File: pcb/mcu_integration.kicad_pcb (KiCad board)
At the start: 4 copper layers, 90.2 x 95.9 mm, 104 parts, among them IC1 TL7660IDGKR, IC10 AD844_OPAMP_MEL, IC2 TL081IDT, IC3 FOD814_OPTO_NOSHD, IC5 FOD814_OPTO_MEL, IC6 AD844_OPAMP_AL, IC7 FOD814_OPTO_AL, IC8 AD844_OPAMP_NOSHD, IC9 TL081IDT, J4 Conn_01x02, J5 DM3BT-DSF-PEJS, M1 MountingHole_Pad, M2 MountingHole_Pad, M3 MountingHole_Pad, M4 MountingHole_Pad, U1 STM32F103RBTx, U2 REF192_NOSHD, U3 REF192_AL, U4 REF192_MEL, U5 TPS2069CDBVR_MOSFET, U6 LM35DM

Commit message: Fixed PCB silkscreen
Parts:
- moved C45 0.19 mm to (156.0, 69.6)
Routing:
- net GND: track 183.5 -> 182.1 mm

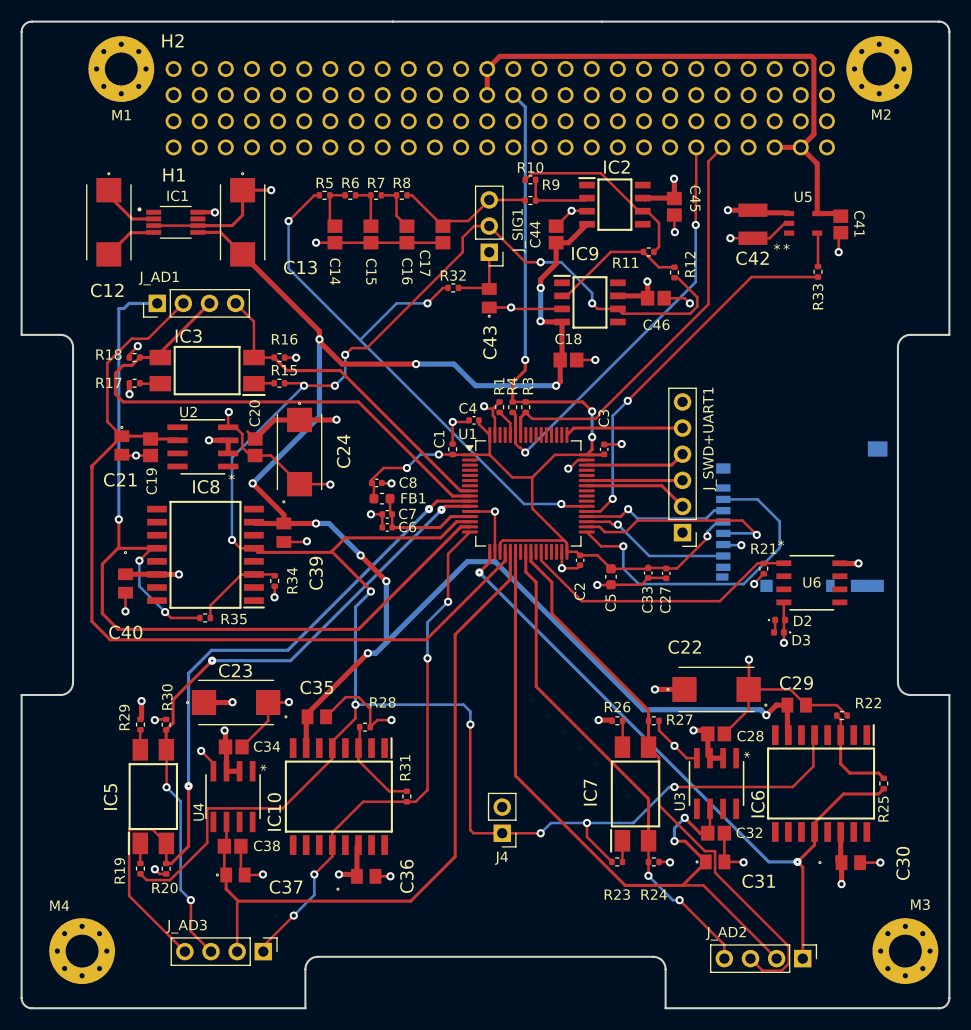
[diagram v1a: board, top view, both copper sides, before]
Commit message: Added silkscreen and changed diode footprints
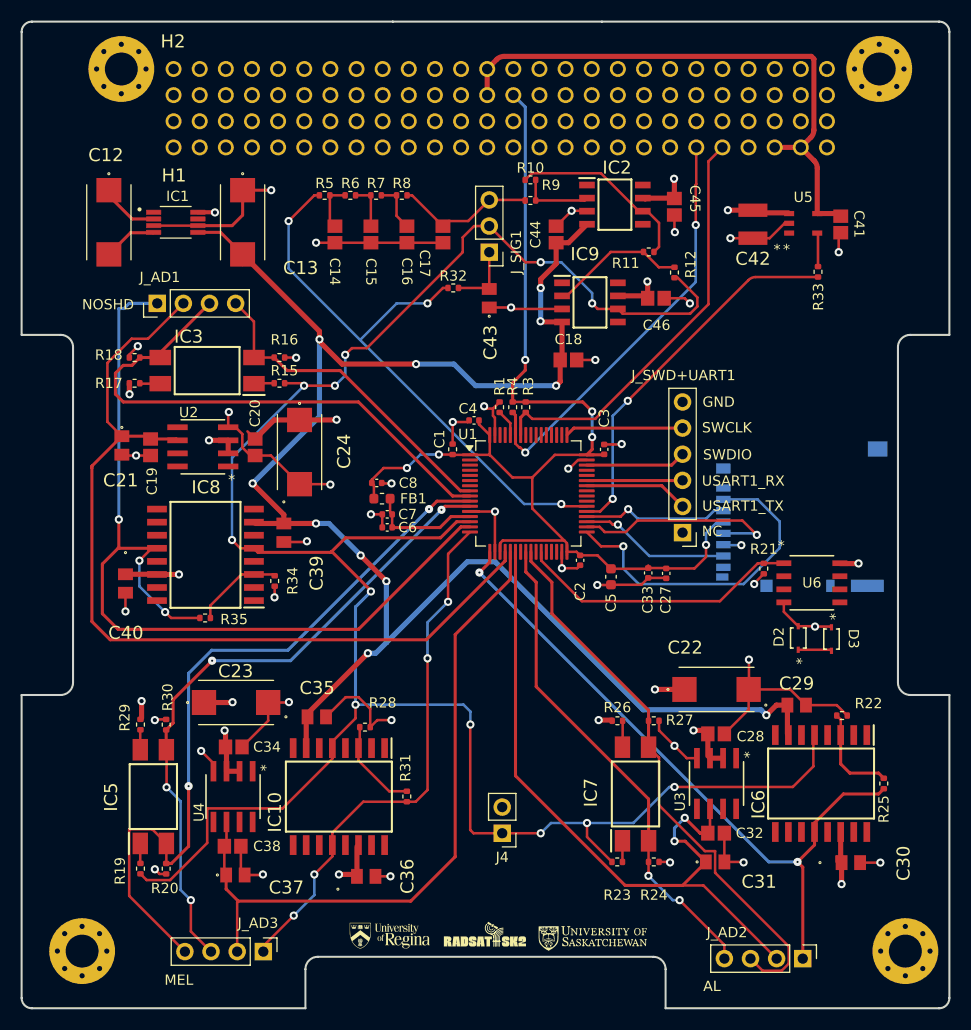
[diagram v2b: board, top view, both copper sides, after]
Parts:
- D2, D3: footprint Diode_SMD:D_0402_1005Metric -> capstone:SOD-323_1P7X1P25_ONS
- moved D3 5.15 mm to (171.3, 111.6), turned to -90 degrees
- moved D2 2.48 mm to (168.0, 111.5), turned to 90 degrees
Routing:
- net GND: track 182.1 -> 184.3 mm
- net DIODE_NET: track 1.41 -> 3.27 mm
- net 3.3V Output: track 109.1 -> 110.1 mm
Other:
- board text added: "AL"
- board text added: "CUBICS Analog IC Shielding Payload REV C Hunter Gerbrandt, Owen Markewich"
- board text added: "GND"
- board text added: "MEL"
- board text added: "NC"
- board text added: "NOSHD"
- board text added: "SWCLK"
- board text added: "SWDIO"
- board text added: "USART1_RX"
- board text added: "USART1_TX"

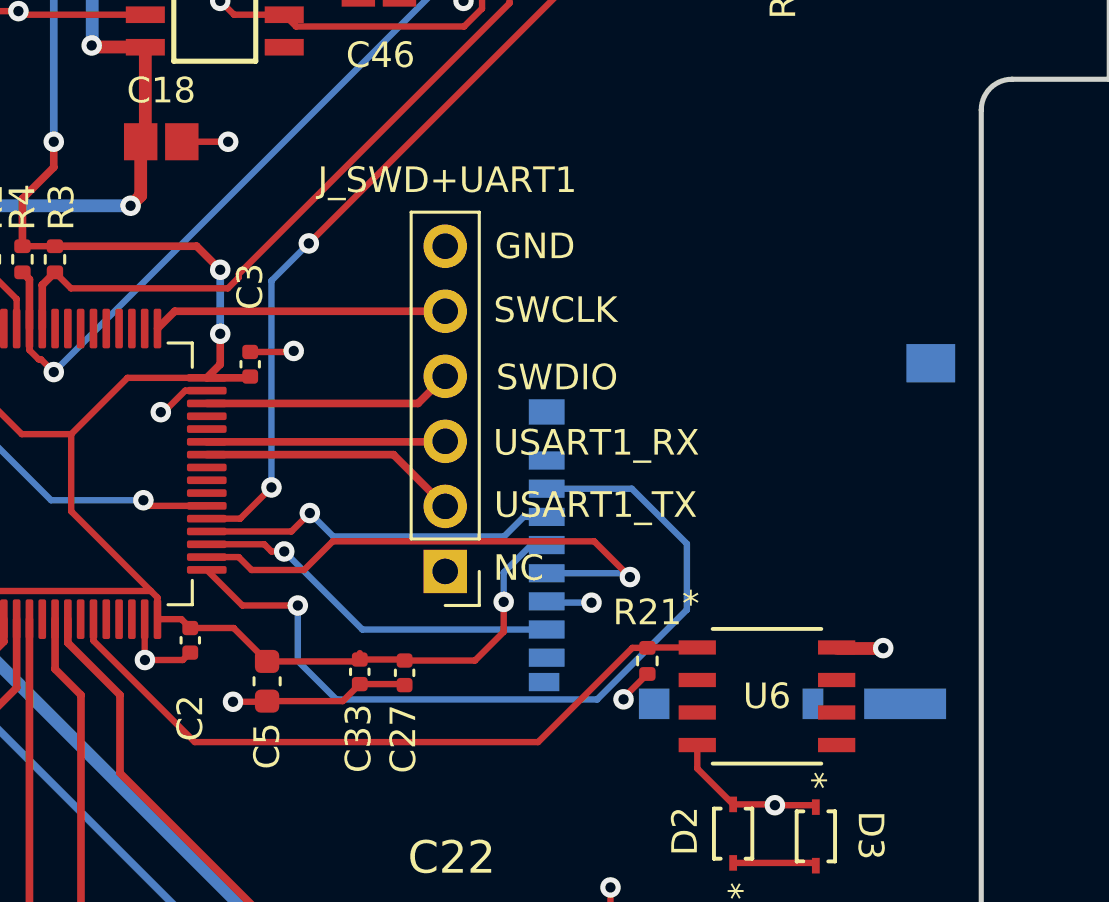
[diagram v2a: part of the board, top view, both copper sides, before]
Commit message: Added reset button & LED, fixed SD card overhang
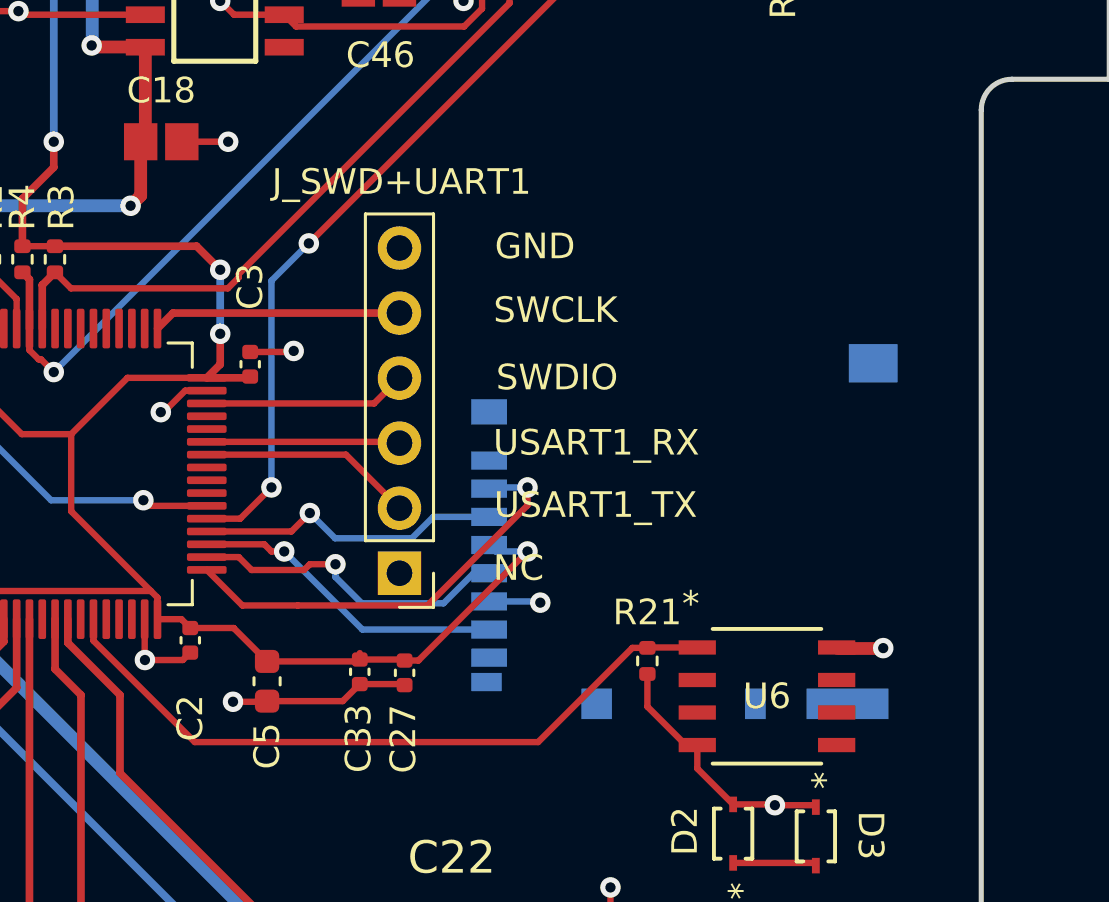
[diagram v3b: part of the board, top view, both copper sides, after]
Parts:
- C14, C15, C16, C17: value 0.1u -> 0.01u
- moved J5 2.25 mm to (166.3, 99.7)
- moved J_SWD+UART1 1.79 mm to (155.0, 101.3)
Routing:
- net /SPI2_CS_NSS: track 32.5 -> 16.9 mm
- net /SPI2_SCK: track 21.1 -> 12.7 mm
- net GND: track 184.3 -> 186.8 mm, vias 41 -> 40
- net /SPI2_MISO: track 14.7 -> 12.4 mm
- net /SPI2_MOSI: track 14.3 -> 12.1 mm
- net /SWDIO: track 9.75 -> 7.94 mm
- net /SWCLK: track 11.5 -> 9.70 mm
- net /USART1_RX: track 9.32 -> 7.55 mm
- net /USART1_TX: track 10.1 -> 8.39 mm
- net 3.3V Output: track 110.1 -> 109.5 mm

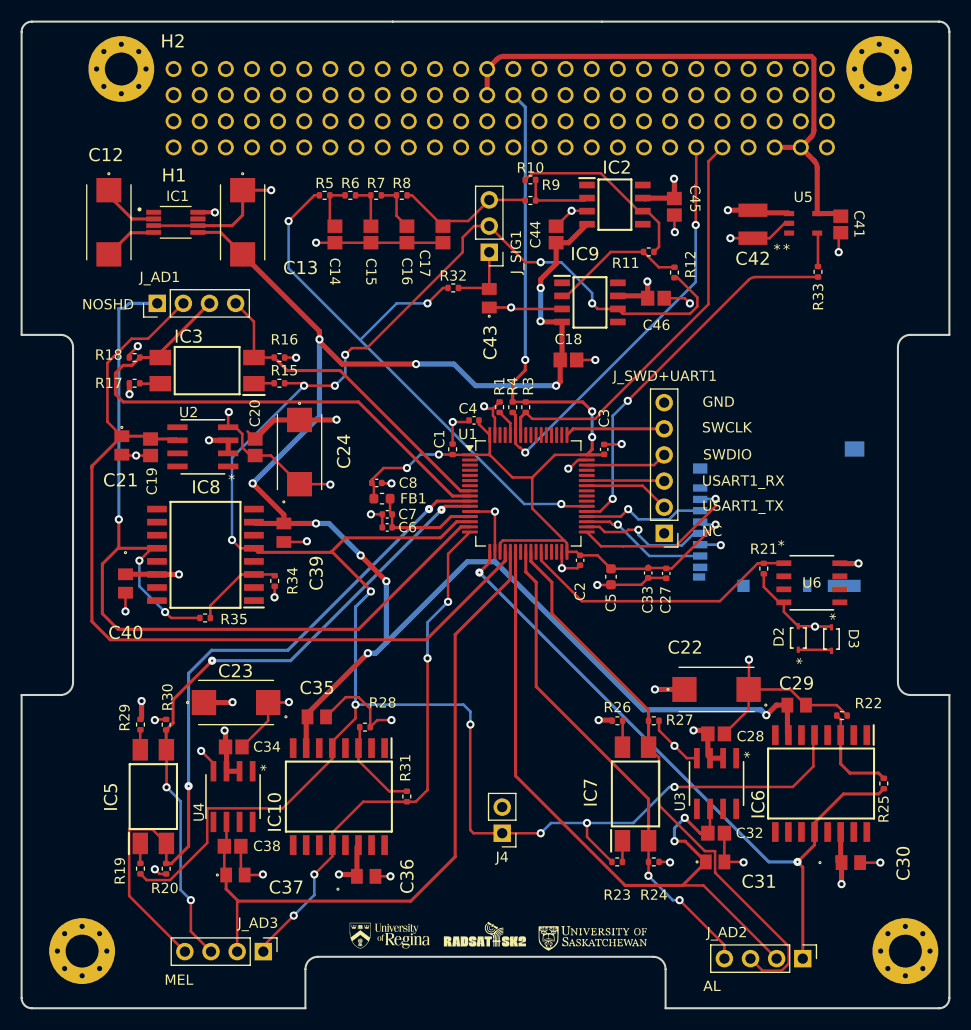
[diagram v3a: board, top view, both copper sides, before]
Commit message: Added reset button & LED, fixed SD card overhang
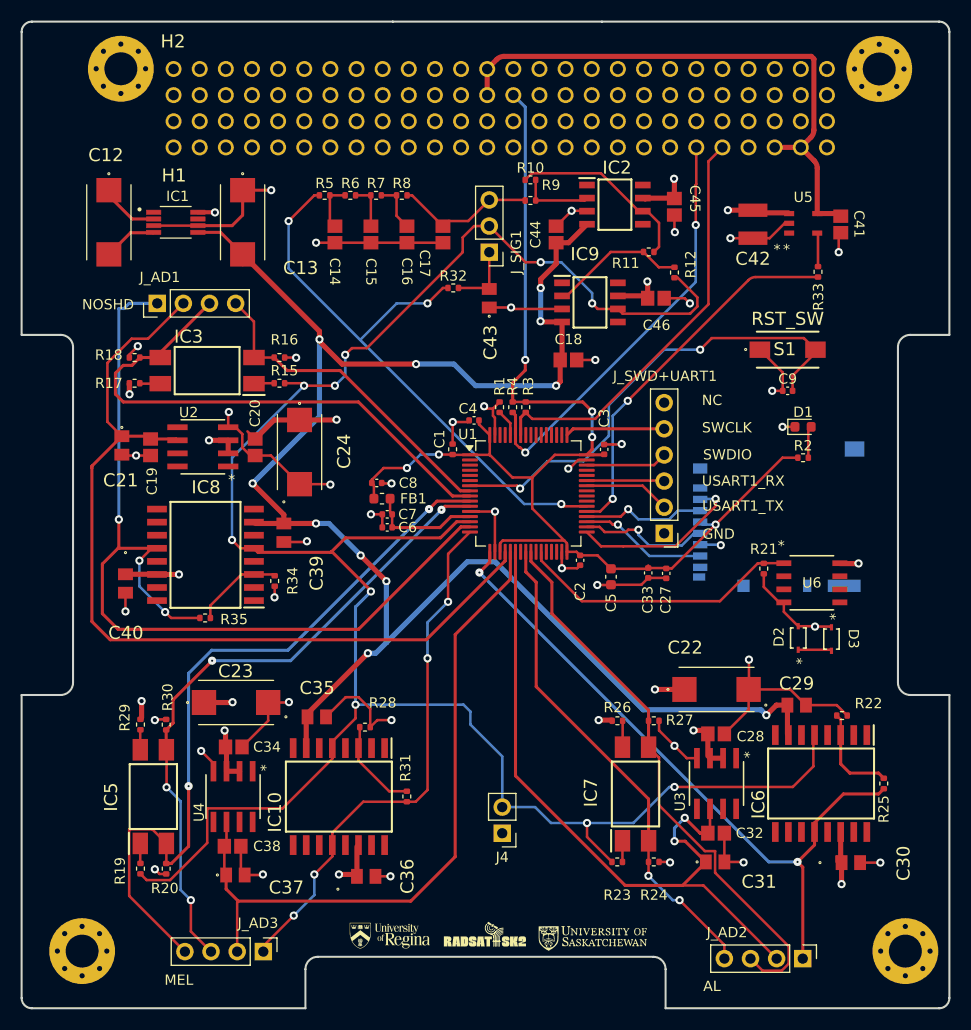
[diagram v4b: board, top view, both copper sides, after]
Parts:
- added C9: 100n, Capacitor_SMD:C_0402_1005Metric, F.Cu at (167.0, 87.5)
- added D1: RED, LED_SMD:LED_0603_1608Metric, F.Cu at (168.5, 91.0)
- added R2: 2.2k, Resistor_SMD:R_0402_1005Metric, F.Cu at (168.5, 94.0)
- added S1: RST_SW, capstone:95C04A3GWRT, F.Cu at (167.0, 83.5)
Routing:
- net /NRST: track 0.00 -> 46.9 mm, vias 0 -> 2
- net 3.3V Output: track 109.5 -> 120.2 mm
- net GND: track 186.8 -> 193.9 mm, vias 40 -> 42
- net ADC1_IN0_SINE: track 215.7 -> 211.8 mm, vias 12 -> 10
- net Net-(D1-A): track 0.00 -> 3.11 mm

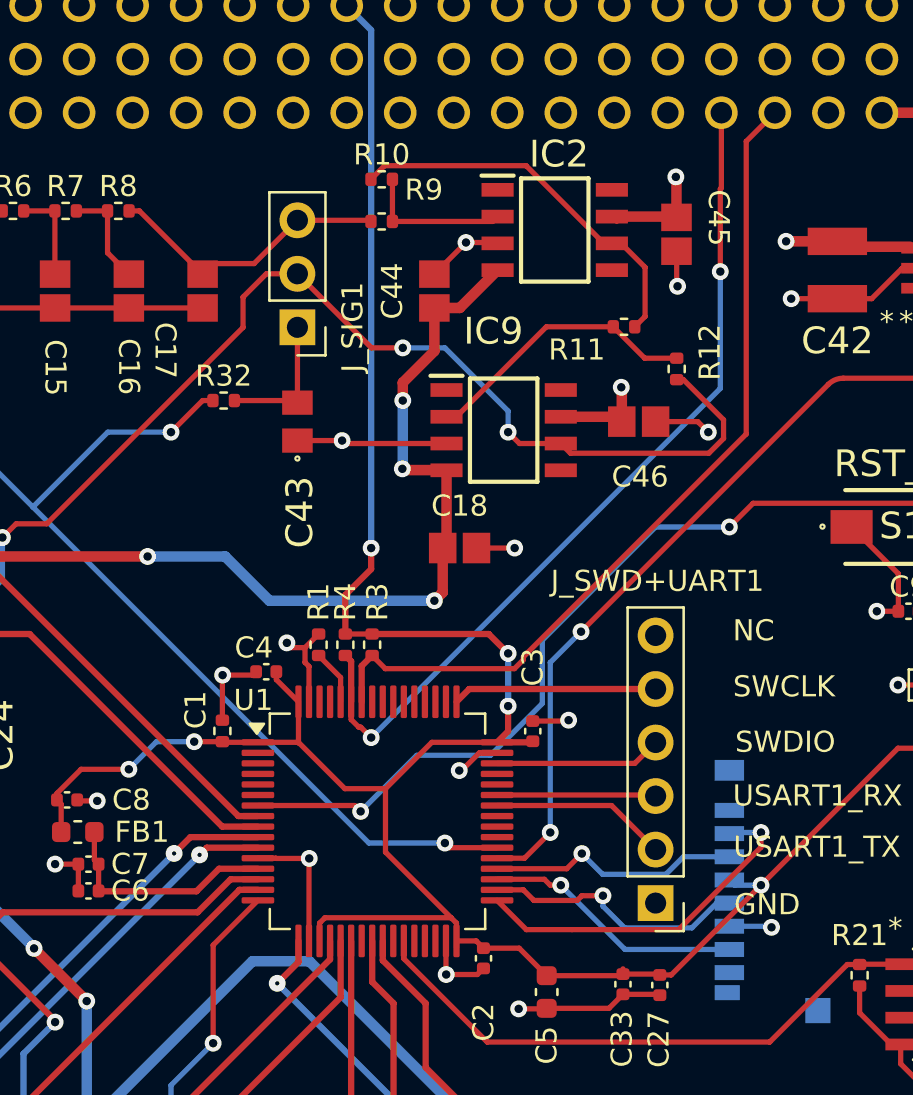
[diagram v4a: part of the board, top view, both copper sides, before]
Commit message: Added non-inverting amplifier to RC Ladder and Changed header pin
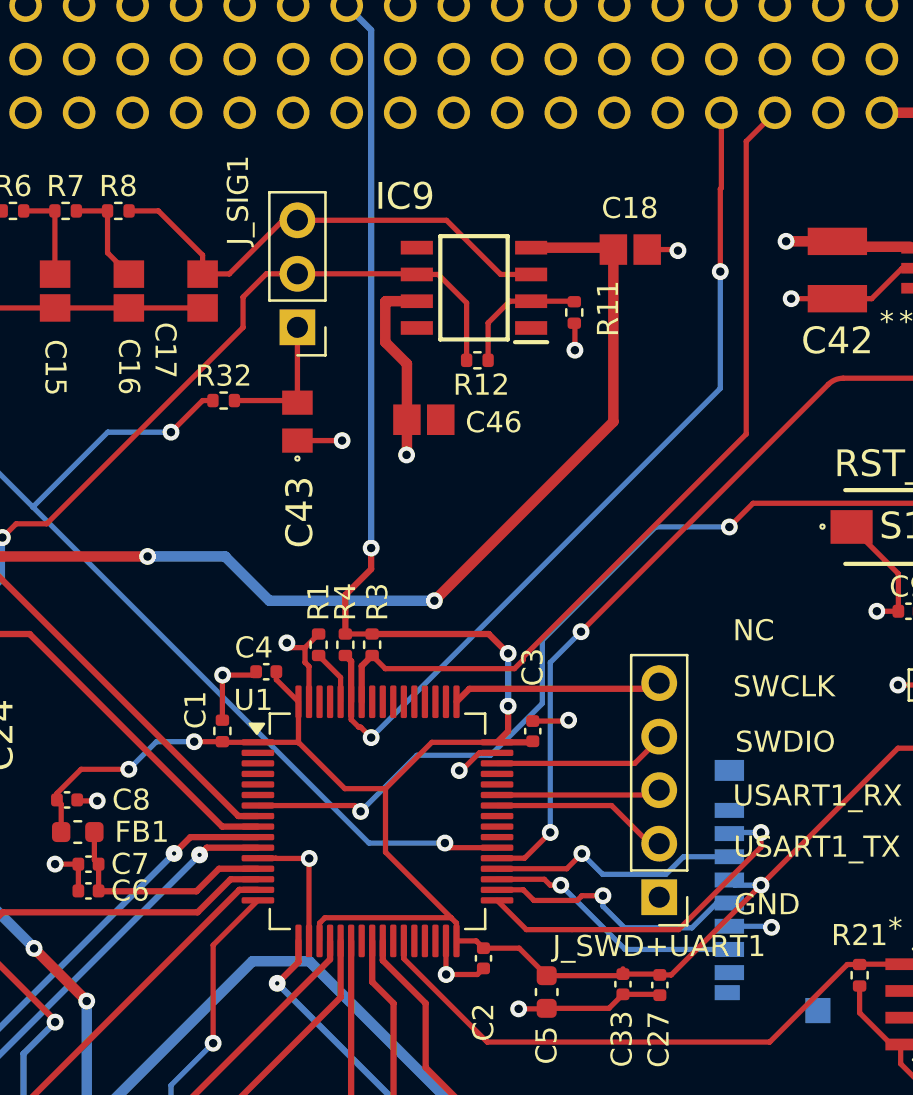
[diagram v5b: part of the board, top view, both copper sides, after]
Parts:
- removed C44, C45: 0.1u, capstone:CAPC220145_88N_KEM-0.1u
- removed IC2: TL081IDT, capstone:SOIC127P600X175-8N
- removed R10: 15K, Resistor_SMD:R_0402_1005Metric
- removed R9: 10K, Resistor_SMD:R_0402_1005Metric
- J_SWD+UART1: value Conn_01x06 -> J_SWD+UART1; footprint Connector_PinHeader_2.54mm:PinHeader_1x06_P2.54mm_Vertical -> Connector_PinHeader_2.54mm:PinHeader_1x05_P2.54mm_Vertical
- R11: value 10K -> 1K
- R12: value 10K -> 9K
- moved C18 16.3 mm to (153.8, 70.3)
- moved C46 10.2 mm to (144.0, 78.4)
- moved R12 9.47 mm to (146.5, 75.6), turned to 0 degrees
- moved IC9 6.90 mm to (146.4, 72.2), turned to 180 degrees
- moved R11 2.46 mm to (151.1, 73.3), turned to -90 degrees
- moved J_SWD+UART1 0.33 mm to (155.2, 101.1)
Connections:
- IC9 pad 3: GND -> RC_OUTPUT
- J_SWD+UART1 pad 1: unconnected-(J_SWD+UART1-Pin_1-Pad1) -> GND
- R11 pad 2: INVERT_SINE -> GND
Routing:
- net INVERT_SINE: track 18.7 -> 0.00 mm
- net ADC1_IN0_SINE: track 211.8 -> 194.6 mm, vias 10 -> 8
- net GND: track 193.9 -> 182.0 mm, vias 42 -> 40
- net RC_OUTPUT: track 13.8 -> 23.0 mm
- net Net-(IC2-INVERTING_INPUT): track 7.09 -> 0.00 mm
- net Net-(IC9-INVERTING_INPUT): track 13.3 -> 6.30 mm
- net -5V Output: track 172.1 -> 175.6 mm, vias 11 -> 9
- net +5V: track 70.7 -> 69.9 mm, vias 17 -> 16
